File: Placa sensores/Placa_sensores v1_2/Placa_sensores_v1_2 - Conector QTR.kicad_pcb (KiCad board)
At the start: 2 copper layers, 15 parts, among them J1 Conn_02x08_Odd_Even, J10 Conn_01x01_Female, J11 Conn_01x01_Female, J12 Conn_01x01_Female, J13 Conn_01x01_Female, J2 Conn_01x01_Female, J3 Conn_01x01_Female, J4 Conn_01x01_Female, J5 Conn_01x01_Female, J6 Conn_01x01_Female, J7 Conn_01x01_Female, J8 Conn_01x01_Female, J9 Conn_01x01_Female

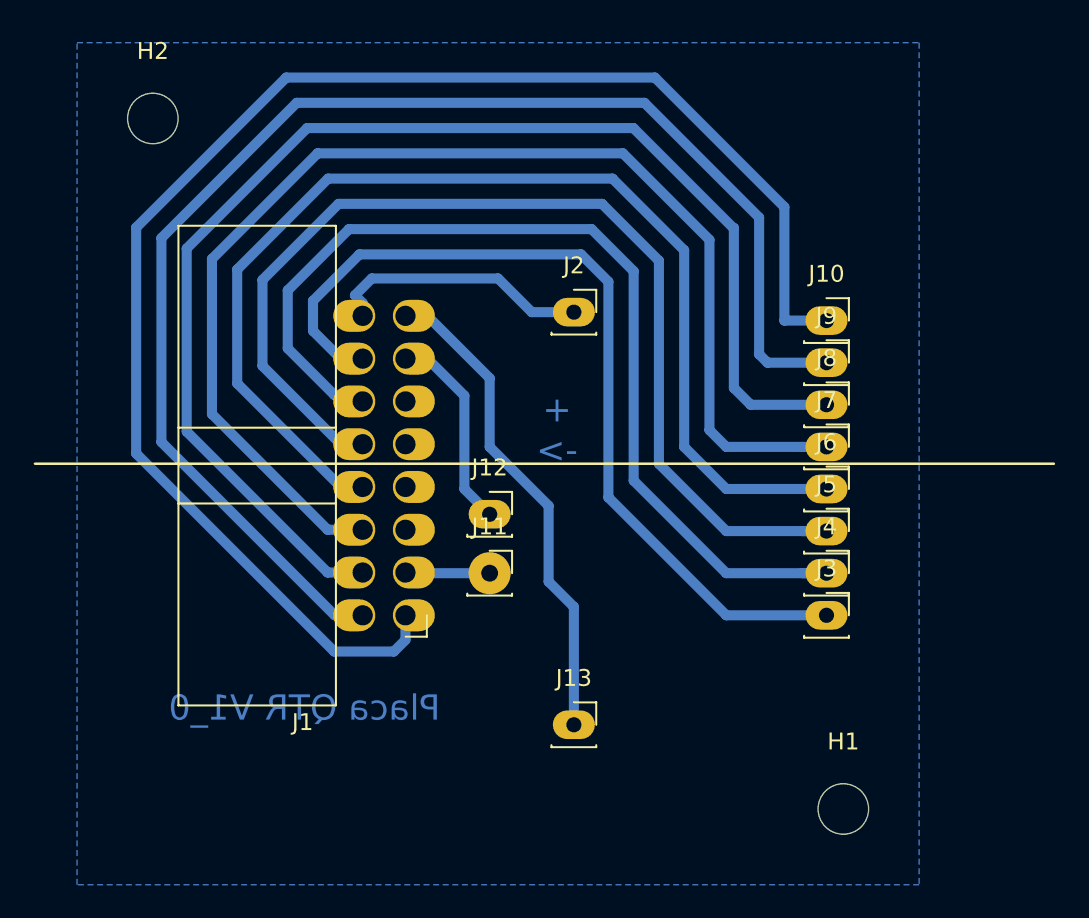
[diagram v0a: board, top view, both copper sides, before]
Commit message: Acertada as placas e os pdfs
Acertada as placas centrais, de alimentação e de conector.
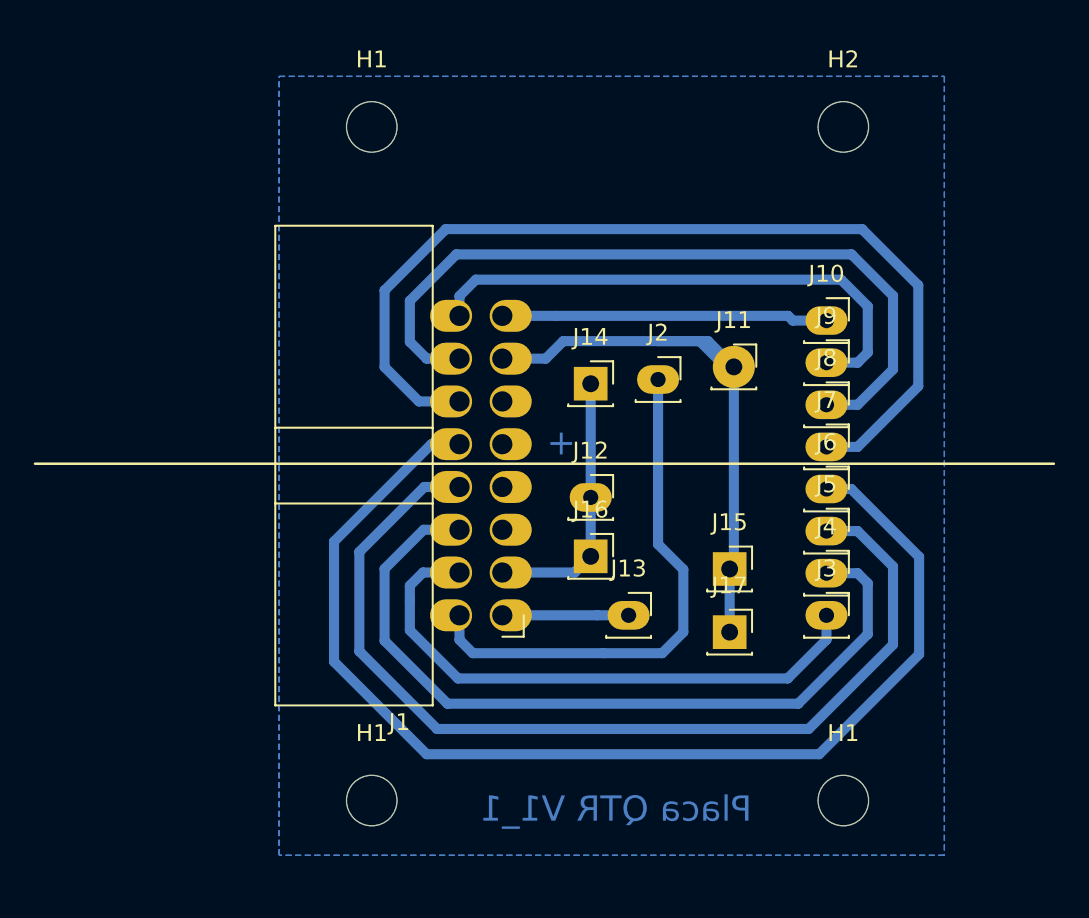
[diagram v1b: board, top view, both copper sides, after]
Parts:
- removed the H1 at (64.5, 67.5)
- added H1: MountingHole, MountingHole:MountingHole_3mm, F.Cu at (36.5, 27.0)
- added H1: MountingHole, MountingHole:MountingHole_3mm, F.Cu at (36.5, 67.0)
- added H1: MountingHole, MountingHole:MountingHole_3mm, F.Cu at (64.5, 67.0)
- added J14: Conn_01x01_Female, Connector_PinSocket_2.54mm:PinSocket_1x01_P2.54mm_Vertical, F.Cu at (49.5, 42.2)
- added J15: Conn_01x01_Female, Connector_PinSocket_2.54mm:PinSocket_1x01_P2.54mm_Vertical, F.Cu at (57.8, 53.2)
- added J16: Conn_01x01_Female, Connector_PinSocket_2.54mm:PinSocket_1x01_P2.54mm_Vertical, F.Cu at (49.5, 52.5)
- added J17: Conn_01x01_Female, Connector_PinSocket_2.54mm:PinSocket_1x01_P2.54mm_Vertical, F.Cu at (57.8, 57.0)
- moved H2 41.0 mm to (64.5, 27.0)
- moved J11 19.0 mm to (58.0, 41.2)
- moved J13 7.27 mm to (51.8, 56.0)
- moved J2 6.40 mm to (53.5, 42.0)
- moved J12 6.08 mm to (49.5, 49.0)
- moved J1 5.75 mm to (44.2, 56.0)
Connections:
- J1 pad 1: Sensor8 -> SensorDir
- J1 pad 10: Sensor3 -> Sensor4
- J1 pad 12: Sensor2 -> Sensor5
- J1 pad 13: VccSensores -> GND
- J1 pad 14: Sensor1 -> Sensor6
- J1 pad 15: SensorDir -> Sensor8
- J1 pad 16: SensorEsq -> Sensor7
- J1 pad 2: Sensor7 -> SensorEsq
- J1 pad 3: GND -> VccSensores
- J1 pad 4: Sensor6 -> Sensor1
- J1 pad 6: Sensor5 -> Sensor2
- J1 pad 8: Sensor4 -> Sensor3
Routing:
- net Sensor8: track 90.6 -> 19.4 mm
- net Sensor7: track 82.3 -> 31.9 mm
- net Sensor6: track 79.5 -> 45.8 mm
- net GND: track 5.02 -> 35.3 mm
- net SensorDir: track 29.2 -> 7.50 mm
- net Sensor1: track 53.4 -> 35.6 mm
- net Sensor5: track 73.9 -> 57.4 mm
- net SensorEsq: track 15.7 -> 31.2 mm
- net Sensor2: track 58.9 -> 47.4 mm
- net Sensor3: track 63.9 -> 58.6 mm
- net VccSensores: track 12.1 -> 15.9 mm
- net Sensor4: track 68.5 -> 69.4 mm
- added copper zone on B.Cu, net (none)
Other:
- board text added: "+"
- board text added: "Placa QTR V1_1"
- board text removed: "+ <-"
- board text removed: "Placa QTR V1_0"
